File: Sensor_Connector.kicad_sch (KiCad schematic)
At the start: 6 parts, among them J501 Sensor_Conn

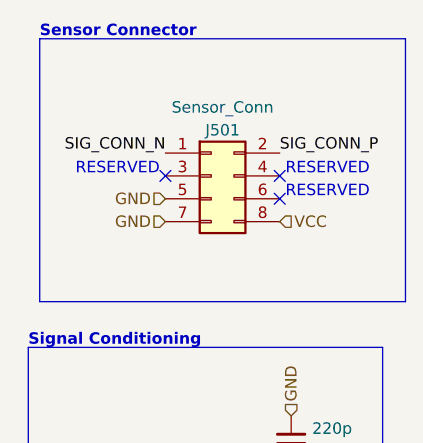
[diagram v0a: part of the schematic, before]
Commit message: (sch) change to ampenol conn
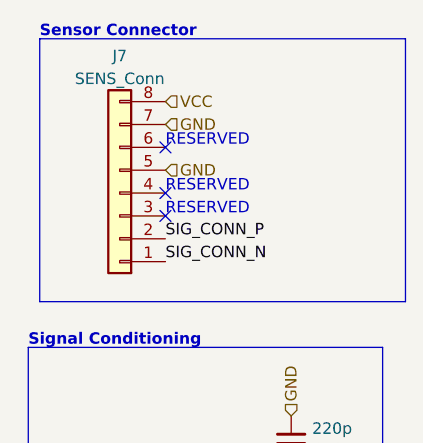
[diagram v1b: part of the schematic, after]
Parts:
- removed J501: Sensor_Conn, grootvoet:TE_7-215079-8, symbol Connector_Generic:Conn_02x04_Odd_Even
- added J7: SENS_Conn, grootvoet:Connector_Amphenol_10114828-xxx08LF_Vertical, symbol Connector_Generic:Conn_01x08
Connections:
- net GND: now also J7.5 (Pin_5), J7.7 (Pin_7)
- net SIG_CONN_N: now also J7.1 (Pin_1)
- net SIG_CONN_P: now also J7.2 (Pin_2)
- net VCC: now also J7.8 (Pin_8)

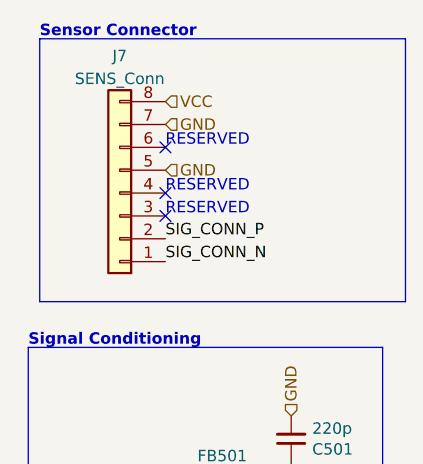
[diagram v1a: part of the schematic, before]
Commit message: (sch) change to 4-pin sens. conn.
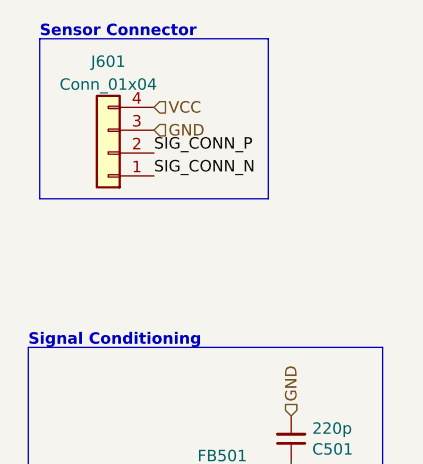
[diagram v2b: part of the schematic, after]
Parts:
- removed J7: SENS_Conn, grootvoet:Connector_Amphenol_10114828-xxx08LF_Vertical, symbol Connector_Generic:Conn_01x08
- added J601: Conn_01x04, symbol Connector_Generic:Conn_01x04
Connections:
- net GND: now also J601.3 (Pin_3)
- net SIG_CONN_N: now also J601.1 (Pin_1)
- net SIG_CONN_P: now also J601.2 (Pin_2)
- net VCC: now also J601.4 (Pin_4)
- no-connect marks 3 -> 0
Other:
- note removed: "RESERVED"
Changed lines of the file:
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@@
   (junction (at 46.99 69.215) (diameter 0) (color 0 0 0 0)
   )
-  (no_connect (at 33.02 36.83))
-  (no_connect (at 33.02 29.21))
-  (no_connect (at 33.02 34.29))
   (wire (pts (xy 49.53 80.645) (xy 46.99 80.645))
     (stroke (width 0) (type default))
   )
-  (polyline (pts (xy 19.05 17.145) (xy 19.05 46.355))
+  (polyline (pts (xy 19.05 17.145) (xy 19.05 34.925))
     (stroke (width 0) (type default))
   )
@@
     (stroke (width 0) (type default))
   )
-  (polyline (pts (xy 19.05 46.355) (xy 59.69 46.355))
+  (polyline (pts (xy 19.05 34.925) (xy 44.45 34.925))
     (stroke (width 0) (type default))
   )
@@
     (stroke (width 0) (type default))
   )
-  (polyline (pts (xy 59.69 17.145) (xy 59.69 46.355))
-    (stroke (width 0) (type default))
-  )
-  (polyline (pts (xy 59.69 17.145) (xy 19.05 17.145))
+  (polyline (pts (xy 44.45 17.145) (xy 44.45 34.925))
+    (stroke (width 0) (type default))
+  )
+  (polyline (pts (xy 44.45 17.145) (xy 19.05 17.145))
     (stroke (width 0) (type default))
   )
@@
     (effects (font (size 1.27 1.27) (thickness 0.254) bold) (justify left bottom))
   )
-  (text "RESERVED" (at 33.02 34.29 0)
-    (effects (font (size 1.27 1.27)) (justify left bottom))
-  )
-  (text "RESERVED" (at 33.02 36.83 0)
-    (effects (font (size 1.27 1.27)) (justify left bottom))
-  )
-  (text "RESERVED" (at 33.02 29.21 0)
-    (effects (font (size 1.27 1.27)) (justify left bottom))
-  )
   (text "Signal Conditioning" (at 17.78 51.435 0)
     (effects (font (size 1.27 1.27) (thickness 0.254) bold) (justify left bottom))
   )
-  (label "SIG_CONN_N" (at 33.02 41.91 0) (fields_autoplaced)
+  (label "SIG_CONN_N" (at 31.75 32.385 0) (fields_autoplaced)
     (effects (font (size 1.27 1.27)) (justify left bottom))
   )
@@
     (effects (font (size 1.27 1.27)) (justify right bottom))
   )
-  (label "SIG_CONN_P" (at 33.02 39.37 0) (fields_autoplaced)
+  (label "SIG_CONN_P" (at 31.75 29.845 0) (fields_autoplaced)
     (effects (font (size 1.27 1.27)) (justify left bottom))
   )
@@
     (effects (font (size 1.27 1.27)) (justify left))
   )
-  (hierarchical_label "GND" (shape input) (at 33.02 31.75 0) (fields_autoplaced)
+  (hierarchical_label "GND" (shape input) (at 31.75 27.305 0) (fields_autoplaced)
     (effects (font (size 1.27 1.27)) (justify left))
   )
@@
     (effects (font (size 1.27 1.27)) (justify left))
   )
-  (hierarchical_label "VCC" (shape input) (at 33.02 24.13 0) (fields_autoplaced)
+  (hierarchical_label "VCC" (shape input) (at 31.75 24.765 0) (fields_autoplaced)
     (effects (font (size 1.27 1.27)) (justify left))
   )
   (hierarchical_label "GND" (shape input) (at 46.99 86.995 270) (fields_autoplaced)
     (effects (font (size 1.27 1.27)) (justify right))
-  )
-  (hierarchical_label "GND" (shape input) (at 33.02 26.67 0) (fields_autoplaced)
-    (effects (font (size 1.27 1.27)) (justify left))
   )
   (symbol (lib_id "Device:C_Small") (at 46.99 84.455 0) (mirror x) (unit 1)
@@
     )
   )
-  (symbol (lib_id "Connector_Generic:Conn_01x08") (at 27.94 34.29 180) (unit 1)
+  (symbol (lib_id "Connector_Generic:Conn_01x04") (at 26.67 29.845 180) (unit 1)
     (in_bom yes) (on_board yes) (dnp no) (fields_autoplaced)
-    (property "Reference" "J7" (at 27.94 19.05 0)
-      (effects (font (size 1.27 1.27)))
-    )
-    (property "Value" "SENS_Conn" (at 27.94 21.59 0)
-      (effects (font (size 1.27 1.27)))
-    )
-    (property "Footprint" "grootvoet:Connector_Amphenol_10114828-xxx08LF_Vertical" (at 27.94 34.29 0)
-      (effects (font (size 1.27 1.27)) hide)
-    )
-    (property "Datasheet" "~" (at 27.94 34.29 0)
-      (effects (font (size 1.27 1.27)) hide)
-    )
-    (property "MPN" "" (at 27.94 34.29 0)
-      (effects (font (size 1.27 1.27)) hide)
-    )
-    (property "Mfr." "" (at 27.94 34.29 0)
+    (property "Reference" "J601" (at 26.67 19.685 0)
+      (effects (font (size 1.27 1.27)))
+    )
+    (property "Value" "Conn_01x04" (at 26.67 22.225 0)
+      (effects (font (size 1.27 1.27)))
+    )
+    (property "Footprint" "" (at 26.67 29.845 0)
+      (effects (font (size 1.27 1.27)) hide)
+    )
+    (property "Datasheet" "~" (at 26.67 29.845 0)
       (effects (font (size 1.27 1.27)) hide)
     )
@@
     (pin "3")
     (pin "4")
-    (pin "5")
-    (pin "6")
-    (pin "7")
-    (pin "8")
-    (instances
-      (project "kleinvoet"
-        (path "/4185c36c-c66e-4dbd-be5d-841e551f4885/00000000-0000-0000-0000-00005edf3693"
-          (reference "J7") (unit 1)
-        )
-        (path "/4185c36c-c66e-4dbd-be5d-841e551f4885"
-          (reference "J7") (unit 1)
-        )
-        (path "/4185c36c-c66e-4dbd-be5d-841e551f4885/00000000-0000-0000-0000-00005ef53a66"
-          (reference "J205") (unit 1)
+    (instances
+      (project "kleinvoet"
+        (path "/4185c36c-c66e-4dbd-be5d-841e551f4885/00000000-0000-0000-0000-00005ee5ecad/f1c168a4-8e09-4be7-8226-fa7de49180b9"
+          (reference "J601") (unit 1)
         )
         (path "/4185c36c-c66e-4dbd-be5d-841e551f4885/00000000-0000-0000-0000-00005ee5ecad/00000000-0000-0000-0000-00005ee62c2b"
           (reference "J501") (unit 1)
         )
-        (path "/4185c36c-c66e-4dbd-be5d-841e551f4885/00000000-0000-0000-0000-00005ee5ecad/f1c168a4-8e09-4be7-8226-fa7de49180b9"
-          (reference "J601") (unit 1)
-        )
-        (path "/4185c36c-c66e-4dbd-be5d-841e551f4885/b53619ea-788f-4bc9-9946-594014d7d22c/7d55f5f7-ad99-481b-88b5-315ad3d2b07e"
+        (path "/4185c36c-c66e-4dbd-be5d-841e551f4885/b53619ea-788f-4bc9-9946-594014d7d22c/7d55f5f7-ad99-481b-88b5-315ad3d2b07e"

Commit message: (sch) assign footprint
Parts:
- J601: footprint (none) -> grootvoet:Connector_Amphenol_10114828-xxx04LF_Vertical
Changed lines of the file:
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@@
       (effects (font (size 1.27 1.27)))
     )
-    (property "Footprint" "" (at 26.67 29.845 0)
+    (property "Footprint" "grootvoet:Connector_Amphenol_10114828-xxx04LF_Vertical" (at 26.67 29.845 0)
       (effects (font (size 1.27 1.27)) hide)
     )
@@
       (effects (font (size 1.27 1.27)) hide)
     )
+    (property "MPN" "" (at 26.67 29.845 0)
+      (effects (font (size 1.27 1.27)) hide)
+    )
+    (property "Mfr." "" (at 26.67 29.845 0)
+      (effects (font (size 1.27 1.27)) hide)
+    )

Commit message: (sch) change from handsoldering footprint to normal
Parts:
- R56: footprint Resistor_SMD:R_0402_1005Metric_Pad0.72x0.64mm_HandSolder -> Resistor_SMD:R_0402_1005Metric
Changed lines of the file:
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@@
       (effects (font (size 1.27 1.27)))
     )
-    (property "Footprint" "Resistor_SMD:R_0402_1005Metric_Pad0.72x0.64mm_HandSolder" (at 46.99 74.295 0)
+    (property "Footprint" "Resistor_SMD:R_0402_1005Metric" (at 46.99 74.295 0)
       (effects (font (size 1.27 1.27)) hide)
     )

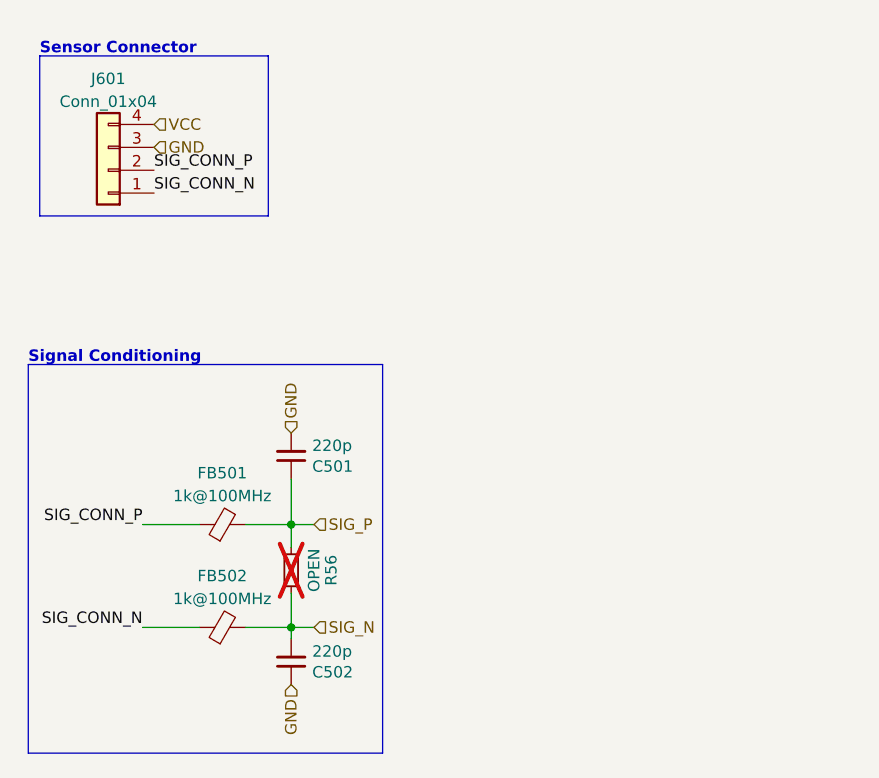
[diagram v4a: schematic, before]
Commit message: (sch) consoldate BOM
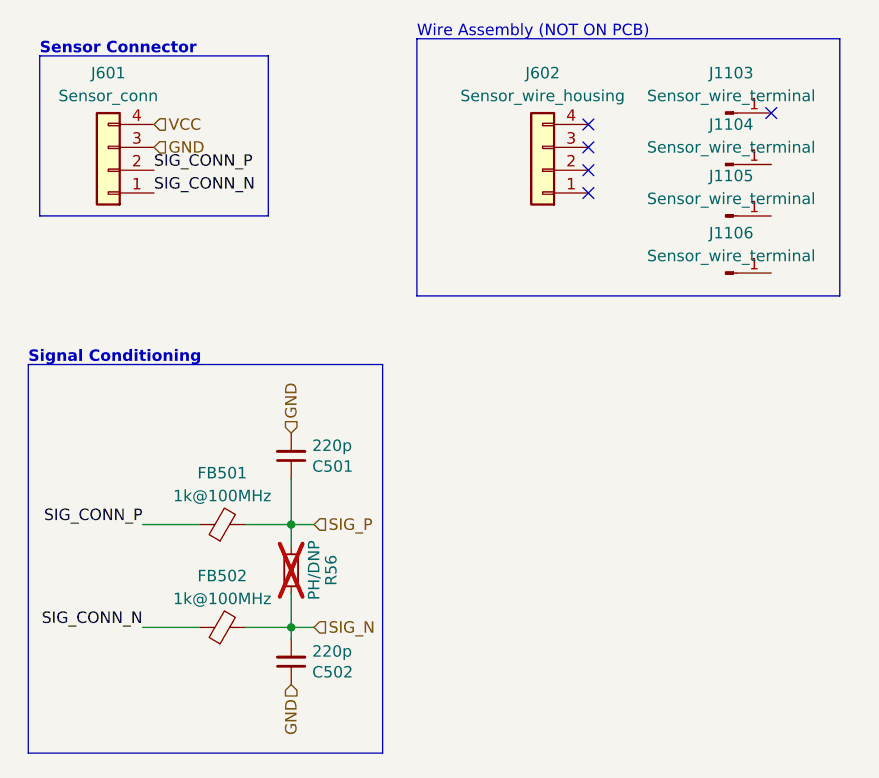
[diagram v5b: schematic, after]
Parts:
- added J1103, J1104, J1105, J1106: Sensor_wire_terminal, symbol Connector:Conn_01x01_Pin
- added J602: Sensor_wire_housing, symbol Connector_Generic:Conn_01x04
- FB501, FB502: MPN (none) -> BLM15AX102SZ1D
- J601: value Conn_01x04 -> Sensor_conn; MPN (none) -> 10114828-11104LF; Mfr. (none) -> Amphenol
- R56: value OPEN -> PH/DNP; MPN DNP -> (none); Mfr. DNP -> (none)
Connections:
- no-connect marks 0 -> 5
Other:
- note added: "Wire Assembly (NOT ON PCB)"

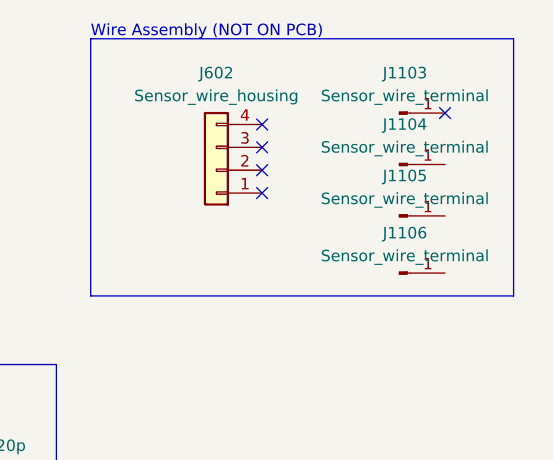
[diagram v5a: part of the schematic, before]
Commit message: (sch) fix connector naming
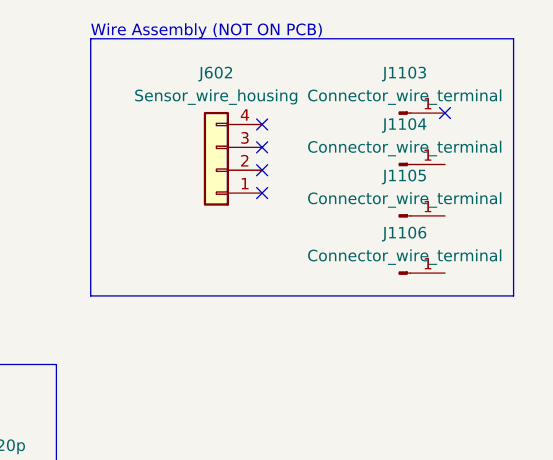
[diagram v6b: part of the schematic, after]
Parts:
- J1103, J1104, J1105, J1106: value Sensor_wire_terminal -> Connector_wire_terminal
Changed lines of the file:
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@@
       (effects (font (size 1.27 1.27)))
     )
-    (property "Value" "Sensor_wire_terminal" (at 95.885 27.305 0)
+    (property "Value" "Connector_wire_terminal" (at 95.885 27.305 0)
       (effects (font (size 1.27 1.27)))
     )
@@
       (effects (font (size 1.27 1.27)))
     )
-    (property "Value" "Sensor_wire_terminal" (at 95.885 21.59 0)
+    (property "Value" "Connector_wire_terminal" (at 95.885 21.59 0)
       (effects (font (size 1.27 1.27)))
     )
@@
       (effects (font (size 1.27 1.27)))
     )
-    (property "Value" "Sensor_wire_terminal" (at 95.885 33.02 0)
+    (property "Value" "Connector_wire_terminal" (at 95.885 33.02 0)
       (effects (font (size 1.27 1.27)))
     )
@@
       (effects (font (size 1.27 1.27)))
     )
-    (property "Value" "Sensor_wire_terminal" (at 95.885 39.37 0)
-      (effects (font (size 1.27 1.27)))
-    )
+    (property "Value" "Connector_wire_terminal" (at 95.885 39.37 0)
+      (effects (font (size 1.27 1.27)))
+    )

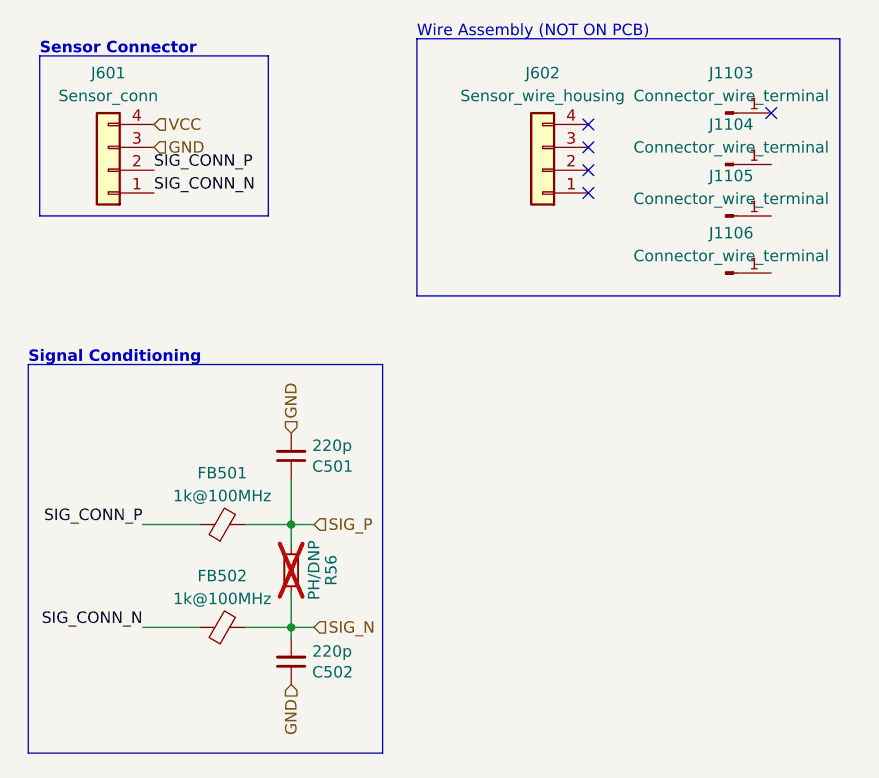
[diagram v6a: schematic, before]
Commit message: (pcb) fix cap footprint & reroute
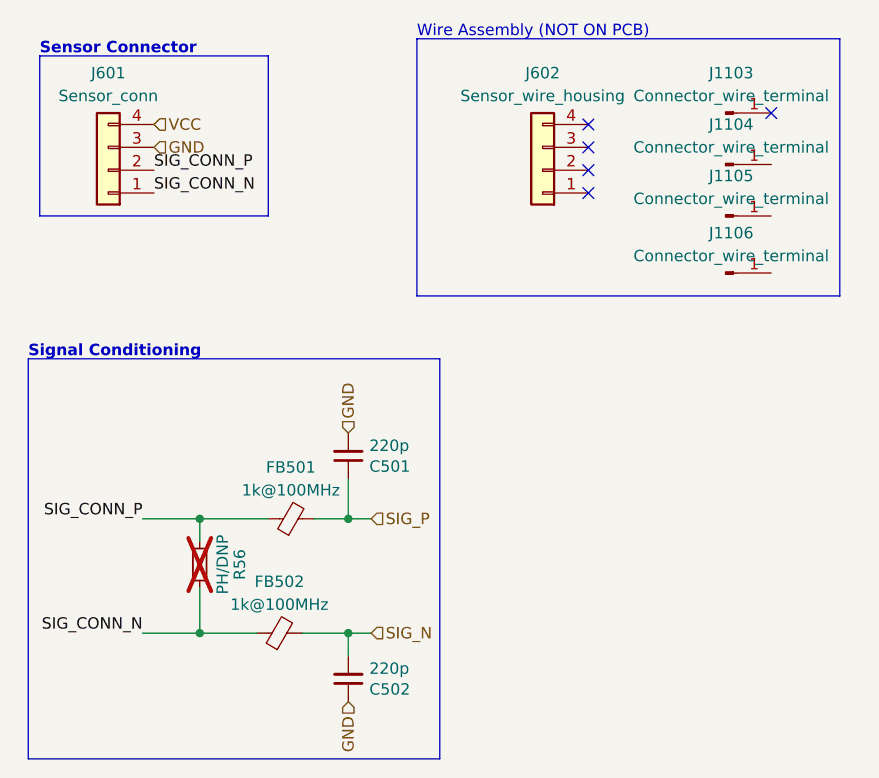
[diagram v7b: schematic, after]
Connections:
- net SIG_CONN_N: now also R56.2
- net SIG_CONN_P: now also R56.1
- net SIG_N: no longer R56.2
- net SIG_P: no longer R56.1
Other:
- moved on the sheet: C501, C502, FB501, FB502, R56
